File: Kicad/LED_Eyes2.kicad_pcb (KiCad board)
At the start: 2 copper layers, 107.8 x 68.3 mm, 18 parts, among them J2 Conn_01x03, U1 74LVC1G17

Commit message: PCB routed
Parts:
- moved C5 0.47 mm to (146.5, 116.8)
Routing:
- net GND: vias 0 -> 16
- added copper zone on B.Cu, net GND
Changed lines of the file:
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@@
     (property "ki_keywords" "capacitor cap")
     (attr smd)
-    (fp_text reference "C6" (at 3.8625 0.4) (layer "F.SilkS")
+    (fp_text reference "C6" (at -0.7375 1.8) (layer "F.SilkS")
         (effects (font (size 1 1) (thickness 0.15)))
     )
@@
     (property "ki_keywords" "RGB LED NeoPixel addressable")
     (attr smd)
-    (fp_text reference "D7" (at 9.63199 -0.5862) (layer "F.SilkS")
+    (fp_text reference "D7" (at 0.05 1.65) (layer "F.SilkS")
         (effects (font (size 1 1) (thickness 0.15)))
     )
@@
         (effects (font (size 1 1) (thickness 0.15)))
     )
-    (fp_text user "1" (at -4.15 -1.6) (layer "F.SilkS")
-        (effects (font (size 1 1) (thickness 0.15)))
-    )
     (fp_text user "${REFERENCE}" (at 0 0) (layer "F.Fab")
         (effects (font (size 0.8 0.8) (thickness 0.15)))
@@
     (property "ki_keywords" "RGB LED NeoPixel addressable")
     (attr smd)
-    (fp_text reference "D5" (at 5.4 1.4) (layer "F.SilkS")
+    (fp_text reference "D5" (at 0.1 -1.7) (layer "F.SilkS")
         (effects (font (size 1 1) (thickness 0.15)))
     )
@@
         (effects (font (size 1 1) (thickness 0.15)))
     )
-    (fp_text user "1" (at -4.15 -1.6) (layer "F.SilkS")
-        (effects (font (size 1 1) (thickness 0.15)))
-    )
     (fp_text user "${REFERENCE}" (at 0 0) (layer "F.Fab")
         (effects (font (size 0.8 0.8) (thickness 0.15)))
@@
     (property "ki_keywords" "RGB LED NeoPixel addressable")
     (attr smd)
-    (fp_text reference "D4" (at -0.05 -11.65 180) (layer "F.SilkS")
+    (fp_text reference "D4" (at 0.05 1.75 180) (layer "F.SilkS")
         (effects (font (size 1 1) (thickness 0.15)))
     )
@@
         (effects (font (size 1 1) (thickness 0.15)))
     )
-    (fp_text user "1" (at -4.15 -1.6) (layer "F.SilkS")
-        (effects (font (size 1 1) (thickness 0.15)))
-    )
     (fp_text user "${REFERENCE}" (at 0 0) (layer "F.Fab")
         (effects (font (size 0.8 0.8) (thickness 0.15)))
@@
     (property "ki_keywords" "RGB LED NeoPixel addressable")
     (attr smd)
-    (fp_text reference "D3" (at -3.95 -3.45) (layer "F.SilkS")
+    (fp_text reference "D3" (at -0.05 1.75) (layer "F.SilkS")
         (effects (font (size 1 1) (thickness 0.15)))
     )
@@
         (effects (font (size 1 1) (thickness 0.15)))
     )
-    (fp_text user "1" (at -4.15 -1.6) (layer "F.SilkS")
-        (effects (font (size 1 1) (thickness 0.15)))
-    )
     (fp_text user "${REFERENCE}" (at 0 0) (layer "F.Fab")
         (effects (font (size 0.8 0.8) (thickness 0.15)))
@@
         (effects (font (size 1 1) (thickness 0.15)))
     )
-    (fp_text user "1" (at -4.15 -1.6) (layer "F.SilkS")
-        (effects (font (size 1 1) (thickness 0.15)))
-    )
     (fp_text user "${REFERENCE}" (at 0 0) (layer "F.Fab")
         (effects (font (size 0.8 0.8) (thickness 0.15)))
@@
   )
   (footprint "Capacitor_SMD:C_0805_2012Metric_Pad1.18x1.45mm_HandSolder" (layer "F.Cu")
-    (at 146.9375 116.8)
+    (at 146.4625 116.8)
     (descr "Capacitor SMD 0805 (2012 Metric), square (rectangular) end terminal, IPC_7351 nominal with elongated pad for handsoldering. (Body size source: IPC-SM-782 page 76, https://www.pcb-3d.com/wordpress/wp-content/uploads/ipc-sm-782a_amendment_1_and_2.pdf, https://docs.google.com/spreadsheets/d/1BsfQQcO9C6DZCsRaXUlFlo91Tg2WpOkGARC1WS5S8t0/edit?usp=sharing), generated with kicad-footprint-generator")
     (tags "capacitor handsolder")
@@
     (property "ki_keywords" "capacitor cap")
     (attr smd)
-    (fp_text reference "C7" (at 0 -1.68) (layer "F.SilkS")
+    (fp_text reference "C7" (at -0.4375 -2.3) (layer "F.SilkS")
         (effects (font (size 1 1) (thickness 0.15)))
     )
@@
     (property "ki_keywords" "connector")
     (attr exclude_from_pos_files)
-    (fp_text reference "J2" (at 4.8 -2.35) (layer "F.SilkS")
+    (fp_text reference "J2" (at -0.1 -3.1) (layer "F.SilkS")
         (effects (font (size 1 1) (thickness 0.15)))
     )
@@
     (property "ki_keywords" "capacitor cap")
     (attr smd)
-    (fp_text reference "C3" (at 0 -1.68) (layer "F.SilkS")
+    (fp_text reference "C3" (at 2.0375 -1.8) (layer "F.SilkS")
         (effects (font (size 1 1) (thickness 0.15)))
     )
@@
         (effects (font (size 1 1) (thickness 0.15)))
     )
-    (fp_text user "1" (at -4.15 -1.6) (layer "F.SilkS")
-        (effects (font (size 1 1) (thickness 0.15)))
-    )
     (fp_text user "${REFERENCE}" (at 0 0) (layer "F.Fab")
         (effects (font (size 0.8 0.8) (thickness 0.15)))
@@
     (property "ki_keywords" "capacitor cap")
     (attr smd)
-    (fp_text reference "C4" (at 0 -1.68) (layer "F.SilkS")
+    (fp_text reference "C4" (at 0 -1.68) (layer "F.SilkS") hide
         (effects (font (size 1 1) (thickness 0.15)))
     )
@@
     (property "ki_keywords" "RGB LED NeoPixel addressable")
     (attr smd)
-    (fp_text reference "D6" (at 0 -3.5) (layer "F.SilkS")
+    (fp_text reference "D6" (at 0.01 1.6) (layer "F.SilkS")
         (effects (font (size 1 1) (thickness 0.15)))
     )
@@
     (property "ki_keywords" "cap capacitor")
     (attr smd)
-    (fp_text reference "C20" (at 2.625 1.9) (layer "F.SilkS")
+    (fp_text reference "C20" (at 0.325 -2.3) (layer "F.SilkS")
         (effects (font (size 1 1) (thickness 0.15)))
     )
@@
   (gr_line (start 145.5 121.9) (end 145.5 124.3)
     (stroke (width 0.2) (type default)) (layer "F.Cu"))
-  (gr_line (start 177 94.4) (end 181.3 94.4)
+  (gr_line (start 177.5 94.4) (end 181.3 94.4)
     (stroke (width 0.2) (type default)) (layer "F.Cu"))
   (gr_line (start 137.7 127.6) (end 137.7 129.9)
@@
   (gr_line (start 137.8 130.2) (end 137.8 131.9)
     (stroke (width 0.2) (type default)) (layer "F.Cu"))
-  (gr_line (start 142.7 116.9) (end 145.8 116.9)
+  (gr_line (start 142.7 116.9) (end 145.4 116.9)
     (stroke (width 0.2) (type default)) (layer "F.Cu"))
   (gr_line (start 121.1 93.5) (end 117.5 93.5)
@@
   (gr_line (start 130.60006 71.7) (end 130.25631 71.6079)
     (stroke (width 0.1) (type solid)) (layer "Edge.Cuts"))
+  (via (at 134.8 127.6) (size 0.6) (drill 0.3) (layers "F.Cu" "B.Cu") (net 2))
+  (via (at 150.3 127.5) (size 0.6) (drill 0.3) (layers "F.Cu" "B.Cu") (net 2))
+  (via (at 177 93.4) (size 0.6) (drill 0.3) (layers "F.Cu" "B.Cu") (net 2))
+  (via (at 112.7 87.3) (size 0.6) (drill 0.3) (layers "F.Cu" "B.Cu") (net 2))
+  (via (at 177 95.3) (size 0.6) (drill 0.3) (layers "F.Cu" "B.Cu") (net 2))
+  (via (at 142.7 127.6) (size 0.6) (drill 0.3) (layers "F.Cu" "B.Cu") (net 2))
+  (via (at 149.9 121.8) (size 0.6) (drill 0.3) (layers "F.Cu" "B.Cu") (net 2))
+  (via (at 131.8 119.7) (size 0.6) (drill 0.3) (layers "F.Cu" "B.Cu") (net 2))
+  (via (at 162.7 87.6) (size 0.6) (drill 0.3) (layers "F.Cu" "B.Cu") (net 2))
+  (via (at 133.9 120.5) (size 0.6) (drill 0.3) (layers "F.Cu" "B.Cu") (net 2))
+  (via (at 137.6 115.1) (size 0.6) (drill 0.3) (layers "F.Cu" "B.Cu") (net 2))
+  (via (at 170.6 95.3) (size 0.6) (drill 0.3) (layers "F.Cu" "B.Cu") (net 2))
+  (via (at 117.6 96.9) (size 0.6) (drill 0.3) (layers "F.Cu" "B.Cu") (net 2))
+  (via (at 167.7 96.7) (size 0.6) (drill 0.3) (layers "F.Cu" "B.Cu") (net 2))
+  (via (at 132.1 133.2) (size 0.6) (drill 0.3) (layers "F.Cu" "B.Cu") (net 2))
+  (via (at 142.6 136.5) (size 0.6) (drill 0.3) (layers "F.Cu" "B.Cu") (net 2))
+  (zone (net 2) (net_name "GND") (layer "B.Cu") (hatch edge 0.5)
+    (connect_pads (clearance 0.5))
+    (min_thickness 0.25) (filled_areas_thickness no)
+    (fill yes (thermal_gap 0.5) (thermal_bridge_width 0.5))
+    (polygon
+      (pts
+        (xy 202.5 67.1)
+        (xy 81.9 67.1)
+        (xy 81.9 143.9)
+        (xy 83.3 145.3)
+        (xy 198 145.3)
+        (xy 202.6 140.7)
+        (xy 202.6 67.2)
+      )
+    )
+  )
   (group "" (id e5b7544f-034c-4cbb-8e5b-55d2115b9b8e)
     (members

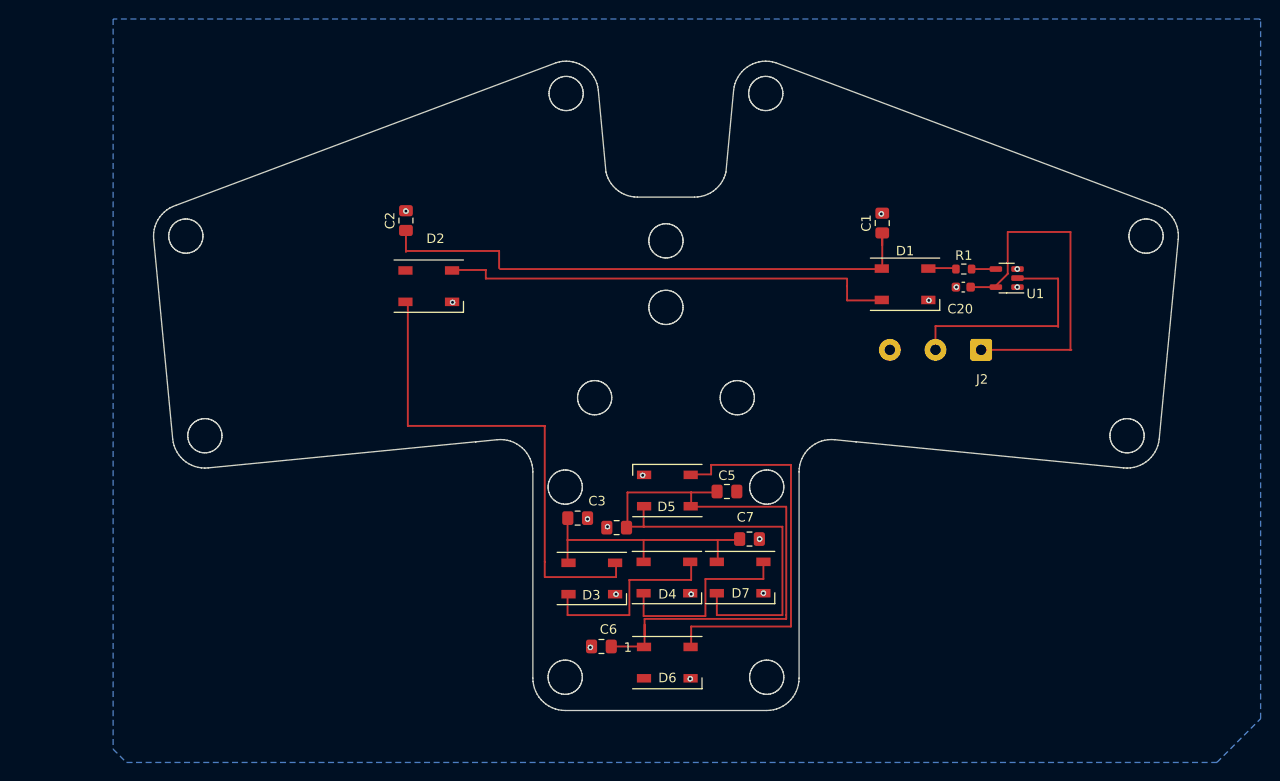
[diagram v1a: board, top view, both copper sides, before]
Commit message: PCB Vorderseite 5V, Rückseite GND
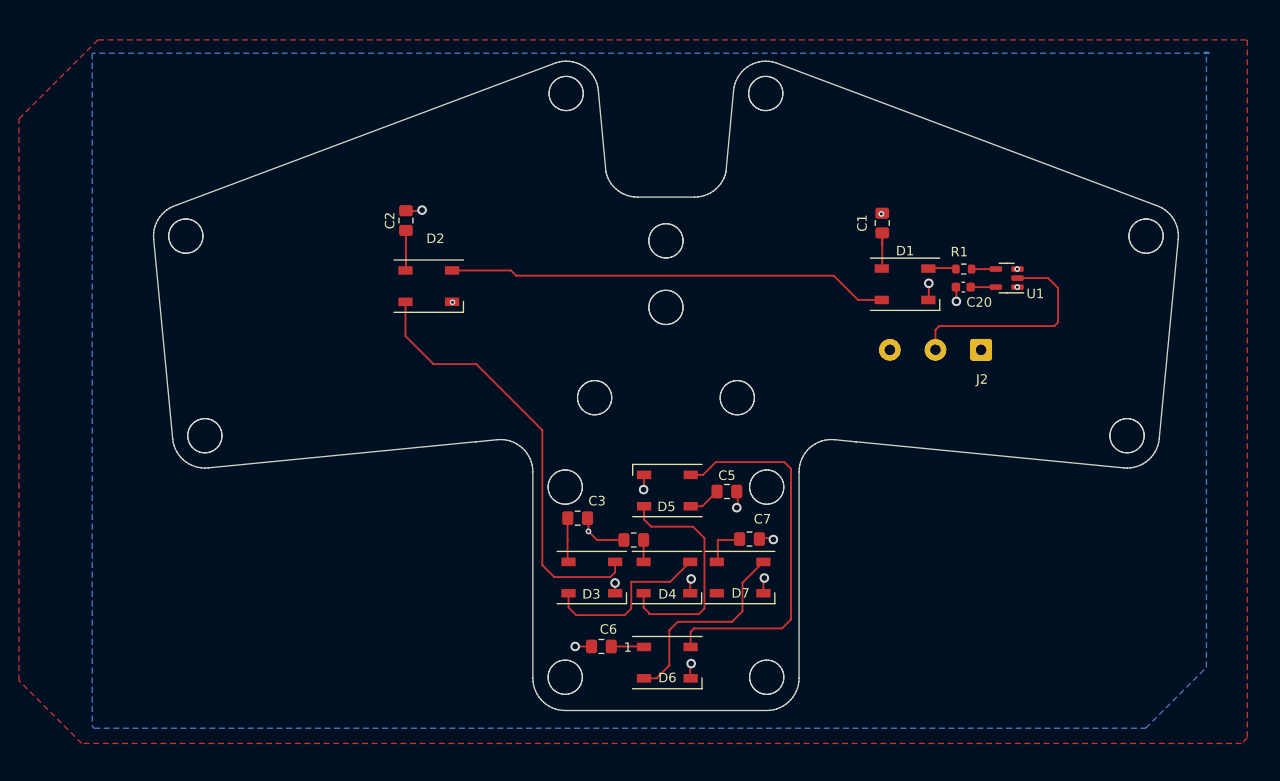
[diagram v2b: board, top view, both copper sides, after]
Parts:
- moved C4 2.22 mm to (136.7, 121.9)
- moved D3 0.10 mm to (132.2, 125.8)
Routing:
- net Net-(D1-DOUT): track 0.00 -> 46.5 mm
- net Net-(D2-DOUT): track 0.00 -> 45.7 mm
- net Net-(D5-DOUT): track 0.00 -> 40.0 mm
- net Net-(D4-DOUT): track 0.00 -> 24.5 mm
- net Net-(J2-Pin_2): track 0.00 -> 23.6 mm
- net Net-(D6-DOUT): track 0.00 -> 21.6 mm
- net Net-(D3-DOUT): track 0.00 -> 18.5 mm
- net GND: track 0.00 -> 7.25 mm
- net +5V: track 0.00 -> 3.57 mm
- added copper zone on F.Cu, net +5V
